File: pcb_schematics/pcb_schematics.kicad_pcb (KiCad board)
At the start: 2 copper layers, 100 x 100 mm, 73 parts, among them J1 Jack, J2 Conn_01x01_Pin, J3 Conn_01x05, J4 Conn_01x05, J5 Conn_01x05, SW1 SW_Push, U1 RPi_Pico_TH, U2 RDA5807M_Module, U3 LM386, U4 LM386

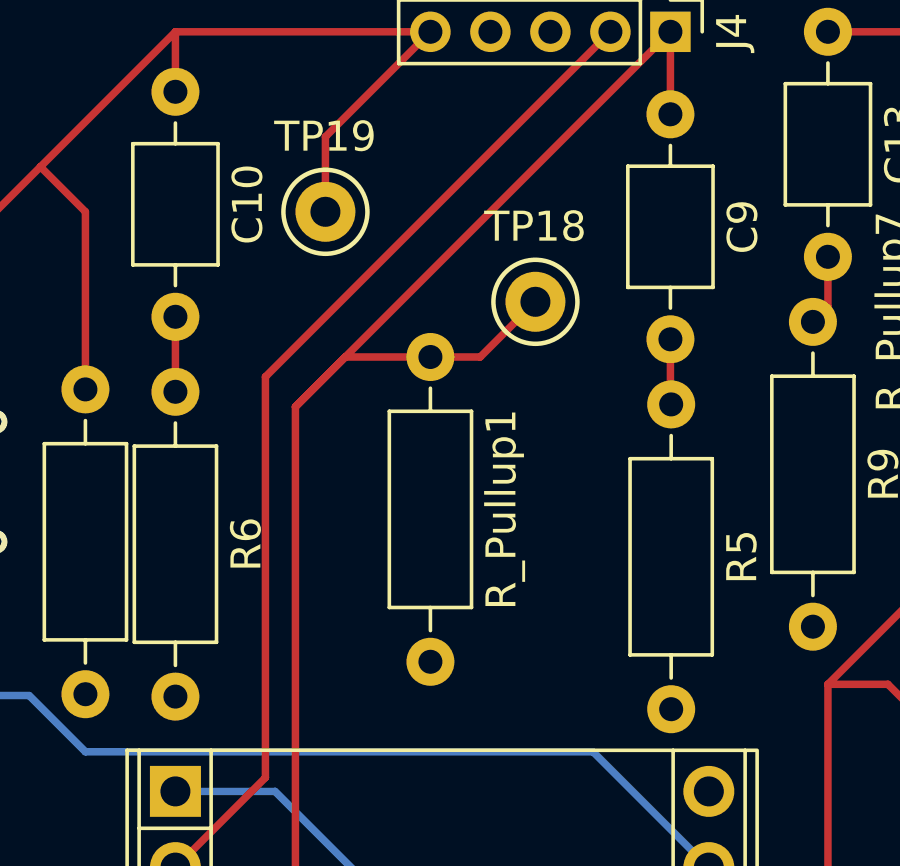
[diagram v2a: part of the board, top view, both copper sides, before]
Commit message: Accomodating usb cable
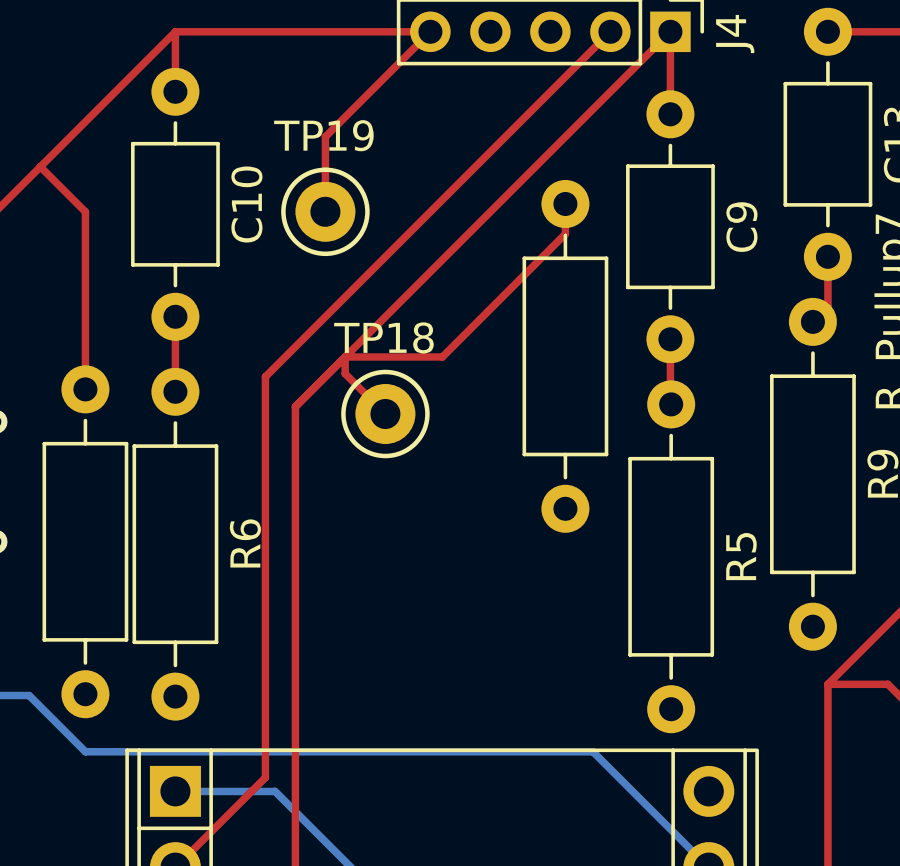
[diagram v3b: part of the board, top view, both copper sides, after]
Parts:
- J1: value Jack -> CUE_SJ1-352XNG
- moved R_Pullup1 6.80 mm to (153.0, 51.0)
- moved TP18 6.24 mm to (147.0, 58.0)
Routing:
- net /ROT1B: track 51.8 -> 57.2 mm
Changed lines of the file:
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@@
   )
   (footprint "TestPoint:TestPoint_Keystone_5000-5004_Miniature" (layer "F.Cu")
-    (at 152 54.26)
+    (at 147 58)
     (descr "Keystone Miniature THM Test Point 5000-5004, http://www.keyelco.com/product-pdf.cfm?p=1309")
     (tags "Through Hole Mount Test Points")
@@
   )
   (footprint "Resistor_THT:R_Axial_DIN0207_L6.3mm_D2.5mm_P10.16mm_Horizontal" (layer "F.Cu")
-    (at 148.5 56.1 -90)
+    (at 153 51 -90)
     (descr "Resistor, Axial_DIN0207 series, Axial, Horizontal, pin pitch=10.16mm, 0.25W = 1/4W, length*diameter=6.3*2.5mm^2, http://cdn-reichelt.de/documents/datenblatt/B400/1_4W%23YAG.pdf")
     (tags "Resistor Axial_DIN0207 series Axial Horizontal pin pitch 10.16mm 0.25W = 1/4W length 6.3mm diameter 2.5mm")
@@
     (property "ki_keywords" "R res resistor")
     (attr through_hole)
-    (fp_text reference "R_Pullup1" (at 5.08 -2.37 90) (layer "F.SilkS")
+    (fp_text reference "R_Pullup1" (at 5.08 -2.37 90) (layer "F.SilkS") hide
         (effects (font (size 1 1) (thickness 0.15)))
     )
@@
         (effects (font (size 1.016 1.016) (thickness 0.1524)) (justify mirror))
     )
-    (fp_text value "Jack" (at 0.5 -8) (layer "B.Fab")
+    (fp_text value "CUE_SJ1-352XNG" (at 0.5 -8) (layer "B.Fab")
         (effects (font (size 1.016 1.016) (thickness 0.1524)) (justify mirror))
     )
@@
   (segment (start 106.25 67.26) (end 106.25 61.51) (width 0.25) (layer "B.Cu") (net 51))
   (segment (start 109.5 58.26) (end 109.5 53.26) (width 0.25) (layer "B.Cu") (net 51))
+  (segment (start 145.66 56.1) (end 144 57.76) (width 0.25) (layer "F.Cu") (net 52))
   (segment (start 156.5 48.01) (end 156.5 45.26) (width 0.25) (layer "F.Cu") (net 52))
   (segment (start 156.5 45.26) (end 144 57.76) (width 0.25) (layer "F.Cu") (net 52))
-  (segment (start 144 57.76) (end 145.66 56.1) (width 0.25) (layer "F.Cu") (net 52))
-  (segment (start 150.16 56.1) (end 148.5 56.1) (width 0.25) (layer "F.Cu") (net 52))
-  (segment (start 152 54.26) (end 150.16 56.1) (width 0.25) (layer "F.Cu") (net 52))
   (segment (start 144 57.76) (end 144 74.136396) (width 0.25) (layer "F.Cu") (net 52))
+  (segment (start 147 58) (end 145.66 56.66) (width 0.25) (layer "F.Cu") (net 52))
+  (segment (start 153 51) (end 153 52) (width 0.25) (layer "F.Cu") (net 52))
+  (segment (start 153 52) (end 148.9 56.1) (width 0.25) (layer "F.Cu") (net 52))
+  (segment (start 145.66 56.66) (end 145.66 56.1) (width 0.25) (layer "F.Cu") (net 52))
+  (segment (start 148.9 56.1) (end 145.66 56.1) (width 0.25) (layer "F.Cu") (net 52))
   (segment (start 140.296396 77.84) (end 140 77.84) (width 0.25) (layer "F.Cu") (net 52))
   (segment (start 144 74.136396) (end 140.296396 77.84) (width 0.25) (layer "F.Cu") (net 52))
-  (segment (start 145.66 56.1) (end 148.5 56.1) (width 0.25) (layer "F.Cu") (net 52))
   (segment (start 156.5 55.51) (end 156.5 57.654763) (width 0.25) (layer "F.Cu") (net 53))
   (segment (start 156.5 57.654763) (end 156.525236 57.679999) (width 0.25) (layer "F.Cu") (net 53))

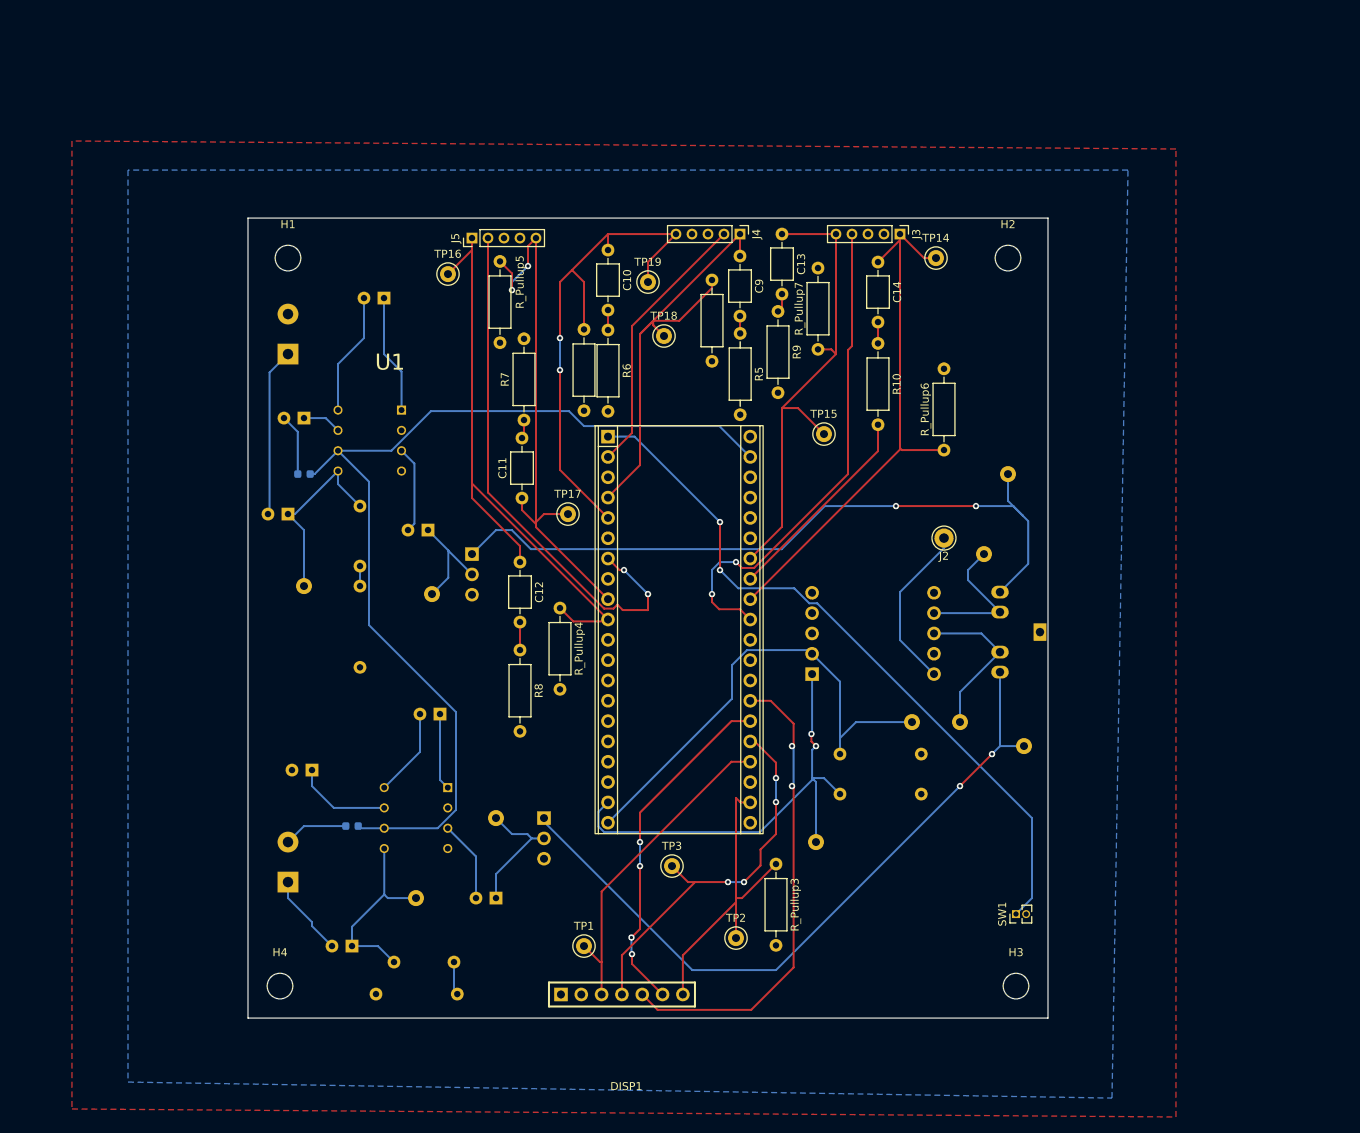
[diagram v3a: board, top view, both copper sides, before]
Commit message: completes third version of PCB
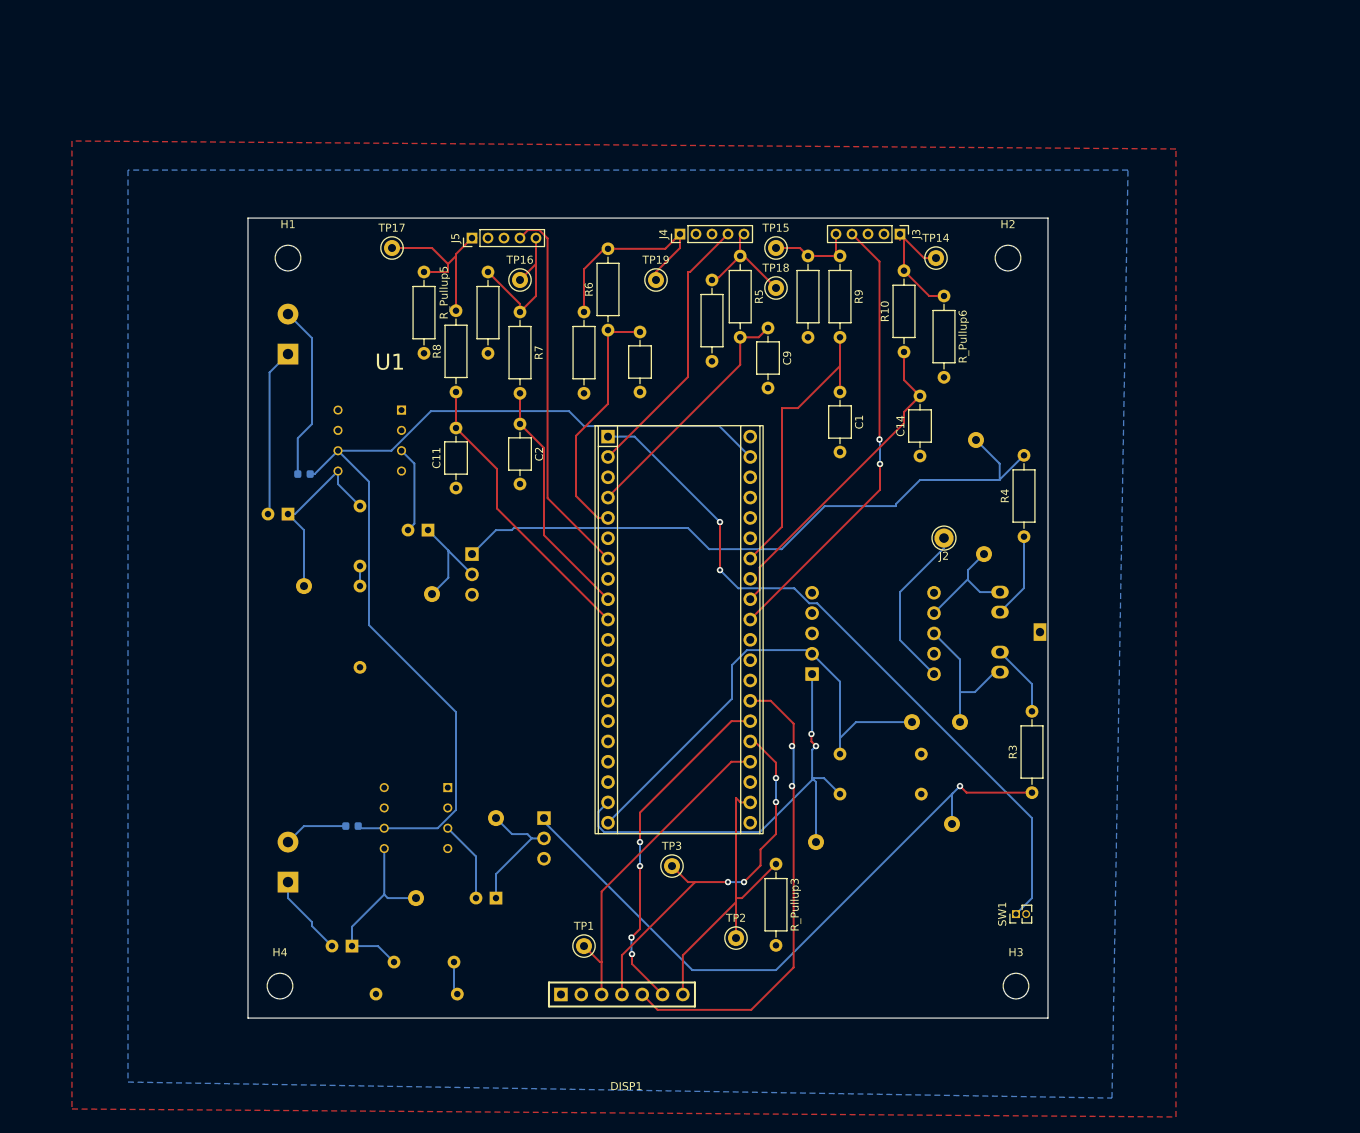
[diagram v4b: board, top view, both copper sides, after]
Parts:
- removed C12, C13: 0.05 µF, Capacitor_THT:C_Axial_L3.8mm_D2.6mm_P7.50mm_Horizontal
- removed C17, C18: 10 µF, Capacitor_THT:CP_Radial_D6.3mm_P2.50mm
- added R3: 10 k, Resistor_THT:R_Axial_DIN0207_L6.3mm_D2.5mm_P10.16mm_Horizontal, F.Cu at (193.0, 115.1)
- added R4: 10 k, Resistor_THT:R_Axial_DIN0207_L6.3mm_D2.5mm_P10.16mm_Horizontal, F.Cu at (192.0, 83.1)
- C1, C2: value 10 µF -> 0.05 µF; footprint Capacitor_THT:CP_Radial_D6.3mm_P2.50mm -> Capacitor_THT:C_Axial_L3.8mm_D2.6mm_P7.50mm_Horizontal; moved to F.Cu
- moved C1 81.2 mm to (169.0, 65.0), turned to -90 degrees
- moved R_Pullup4 43.0 mm to (125.0, 50.0)
- moved TP17 39.9 mm to (113.0, 47.0)
- moved R8 33.2 mm to (121.0, 65.0), turned to 90 degrees
- moved C2 27.0 mm to (129.0, 69.0), turned to -90 degrees
- moved C14 24.8 mm to (179.0, 73.0), turned to 90 degrees
- moved TP15 24.0 mm to (161.0, 47.0)
- moved R_Pullup6 19.3 mm to (182.0, 53.0), turned to -90 degrees
- moved C10 18.2 mm to (144.0, 65.0), turned to 90 degrees
- moved TP18 15.2 mm to (161.0, 52.0)
- moved R7 13.5 mm to (129.0, 55.0), turned to -90 degrees
- moved TP13 13.3 mm to (183.0, 119.0)
- moved R_Pullup7 11.7 mm to (165.0, 48.0), turned to -90 degrees
- moved R9 10.4 mm to (169.0, 48.0)
- moved R5 9.68 mm to (156.5, 48.0)
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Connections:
- C1 pad 1: Net-(U3-BYPASS) -> /ROT3A
- C10 pad 1: /ROT1A -> GND
- C10 pad 2: Net-(C10-Pad2) -> /ROT1A
- C11 pad 1: /ROT2A -> GND
- C11 pad 2: Net-(C11-Pad2) -> /ROT2B
- C14 pad 1: /ROT3B -> GND
- C14 pad 2: Net-(C14-Pad2) -> /ROT3B
- C2 pad 1: Net-(U4-BYPASS) -> /ROT2A
- C9 pad 2: Net-(C9-Pad2) -> GND
- J1 pad 2: /RSpeaker -> /LOUT
- J1 pad 3: /LSpeaker -> /ROUT
- J1 pad 4: /ROUT -> /RSpeaker
- J1 pad 5: /LOUT -> /LSpeaker
- J3 pad 1: /ROT3B -> Net-(J3-Pin_1)
- J3 pad 5: /ROT3A -> Net-(J3-Pin_5)
- J4 pad 1: /ROT1B -> Net-(J4-Pin_1)
- J4 pad 2: /SW2 -> GND
- J4 pad 4: GND -> /SW2
- J4 pad 5: /ROT1A -> Net-(J4-Pin_5)
- J5 pad 1: /ROT2B -> Net-(J5-Pin_1)
- J5 pad 2: /SW4 -> GND
- J5 pad 4: GND -> /SW4
- J5 pad 5: /ROT2A -> Net-(J5-Pin_5)
- R10 pad 1: Net-(C14-Pad2) -> /ROT3B
- R10 pad 2: GND -> Net-(J3-Pin_1)
- R5 pad 1: Net-(C9-Pad2) -> Net-(J4-Pin_5)
- R5 pad 2: GND -> /ROT1B
- R6 pad 1: Net-(C10-Pad2) -> /ROT1A
- R6 pad 2: GND -> Net-(J4-Pin_1)
- R7 pad 1: Net-(C11-Pad2) -> Net-(J5-Pin_5)
- R7 pad 2: GND -> /ROT2A
- R8 pad 1: Net-(C12-Pad2) -> /ROT2B
- R8 pad 2: GND -> Net-(J5-Pin_1)
- R9 pad 1: Net-(C13-Pad2) -> Net-(J3-Pin_5)
- R9 pad 2: GND -> /ROT3A
- RV1 pad 1: /LSpeaker -> Net-(R3-Pad1)
- RV2 pad 1: /RSpeaker -> Net-(R4-Pad2)
- R_Pullup1 pad 1: /ROT1B -> Net-(J4-Pin_5)
- R_Pullup2 pad 1: /ROT1A -> Net-(J4-Pin_1)
- R_Pullup4 pad 1: /ROT2B -> Net-(J5-Pin_5)
- R_Pullup5 pad 1: /ROT2A -> Net-(J5-Pin_1)
- R_Pullup6 pad 1: /ROT3B -> Net-(J3-Pin_1)
- R_Pullup7 pad 1: /ROT3A -> Net-(J3-Pin_5)
- TP12 pad 1: /RSpeaker -> Net-(R4-Pad2)
- TP13 pad 1: /LSpeaker -> Net-(R3-Pad1)
- TP14 pad 1: /ROT3B -> Net-(J3-Pin_1)
- TP15 pad 1: /ROT3A -> Net-(J3-Pin_5)
- TP16 pad 1: /ROT2B -> Net-(J5-Pin_5)
- TP17 pad 1: /ROT2A -> Net-(J5-Pin_1)
- TP18 pad 1: /ROT1B -> Net-(J4-Pin_5)
- TP19 pad 1: /ROT1A -> Net-(J4-Pin_1)
- U3 pad 1: Net-(C17-Pad1) -> unconnected-(U3-GAIN-Pad1)
- U3 pad 7: Net-(U3-BYPASS) -> unconnected-(U3-BYPASS-Pad7)
- U3 pad 8: Net-(C17-Pad2) -> unconnected-(U3-GAIN-Pad8)
- U4 pad 1: Net-(C18-Pad1) -> unconnected-(U4-GAIN-Pad1)
- U4 pad 7: Net-(U4-BYPASS) -> unconnected-(U4-BYPASS-Pad7)
- U4 pad 8: Net-(C18-Pad2) -> unconnected-(U4-GAIN-Pad8)
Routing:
- net Net-(R3-Pad1): track 0.00 -> 82.9 mm, vias 0 -> 1
- net Net-(R4-Pad2): track 0.00 -> 82.6 mm
- net /RSpeaker: track 91.0 -> 10.9 mm, vias 2 -> 0
- net /LSpeaker: track 89.0 -> 9.07 mm, vias 2 -> 0
- net /ROT2B: track 79.6 -> 36.6 mm
- net /ROT2A: track 69.2 -> 30.3 mm, vias 2 -> 0
- net /ROT1A: track 66.4 -> 31.6 mm, vias 2 -> 0
- net /ROT3B: track 69.4 -> 40.5 mm
- net /ROT1B: track 57.2 -> 30.7 mm
- net Net-(J4-Pin_1): track 0.00 -> 25.7 mm
- net /ROT3A: track 60.8 -> 36.7 mm
- net Net-(J5-Pin_1): track 0.00 -> 23.9 mm
- net Net-(J5-Pin_5): track 0.00 -> 22.8 mm
- net /SW4: track 67.1 -> 47.4 mm, vias 2 -> 0
- net Net-(J3-Pin_1): track 0.00 -> 17.6 mm
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
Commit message: fixed issues mentioned by rob and brent
Fix iteration 1
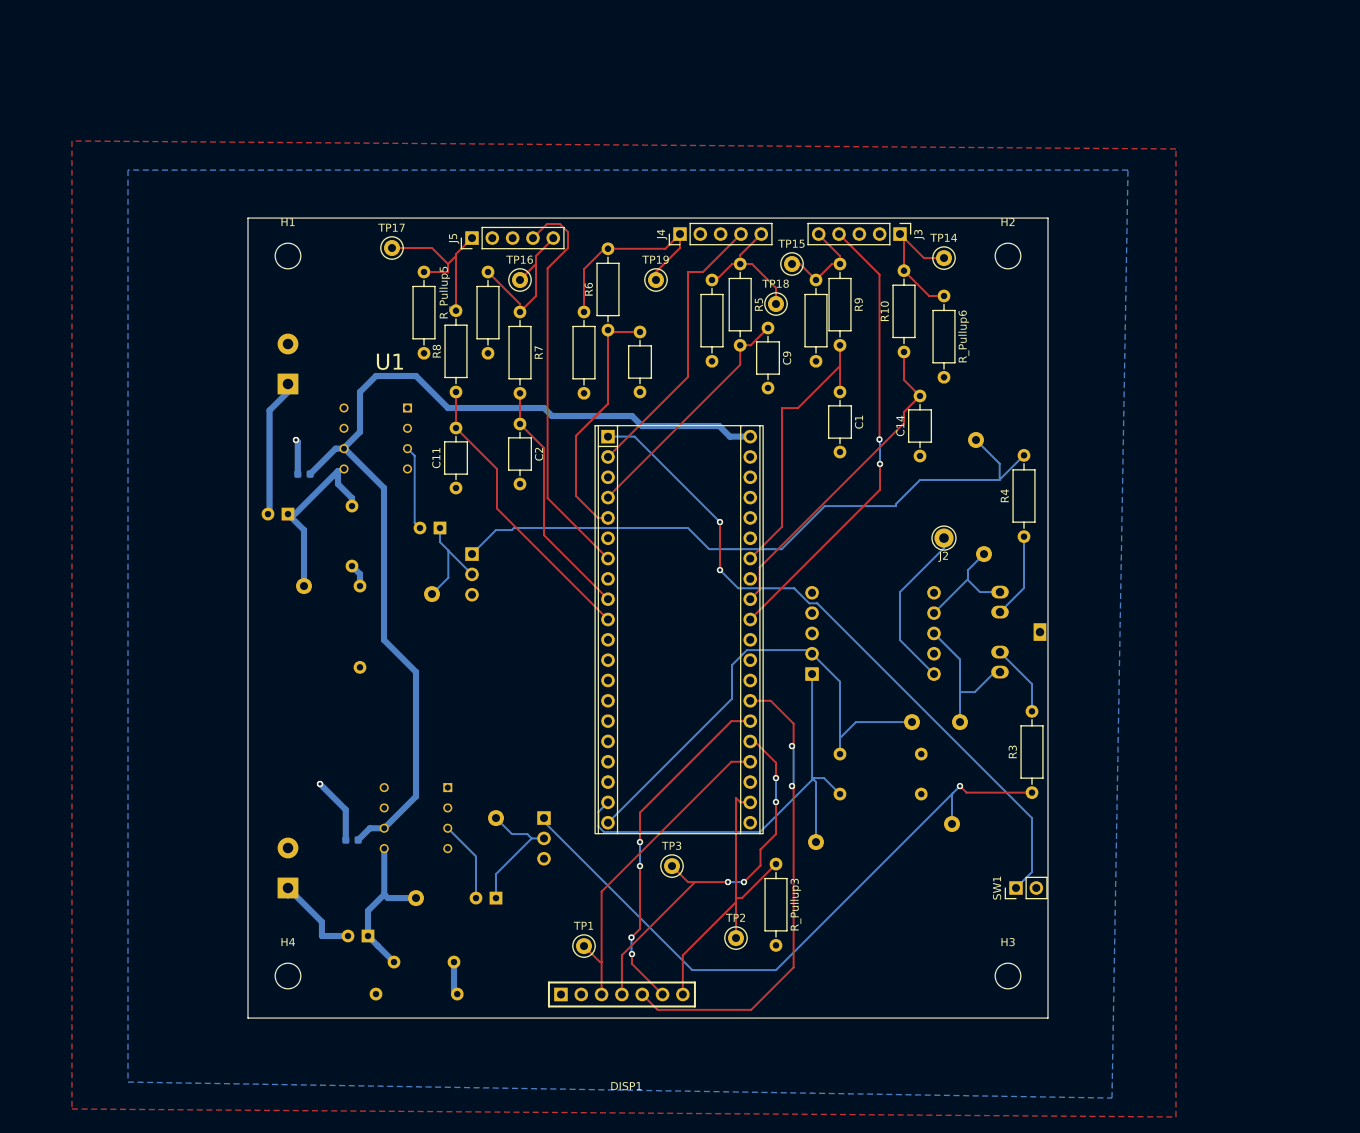
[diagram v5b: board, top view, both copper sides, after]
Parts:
- C1, C10, C11, C14, C2, C9: value 0.05 µF -> 0.01 µF
- J3, J4, J5: footprint Connector_PinHeader_2.00mm:PinHeader_1x05_P2.00mm_Vertical -> Connector_PinHeader_2.54mm:PinHeader_1x05_P2.54mm_Vertical
- R7, R8: value 10Ω -> 10kΩ
- R_Pullup1, R_Pullup2, R_Pullup3, R_Pullup4, R_Pullup5, R_Pullup6, R_Pullup7: value 2kΩ -> 10kΩ
- SW1: footprint Connector_PinHeader_1.27mm:PinHeader_1x02_P1.27mm_Vertical -> Connector_PinHeader_2.54mm:PinHeader_1x02_P2.54mm_Vertical
- moved LS2 3.74 mm to (100.0, 64.0)
- moved SW1 3.26 mm to (191.0, 127.0)
- moved R_Pullup7 3.16 mm to (166.0, 51.0)
- moved TP15 2.83 mm to (163.0, 49.0)
- moved C6 2.36 mm to (110.0, 133.0)
- moved TP18 2.00 mm to (161.0, 54.0)
- moved C8 1.74 mm to (108.0, 121.0)
- moved H3 1.61 mm to (190.0, 138.0)
- moved H4 1.61 mm to (100.0, 138.0)
- moved C16 1.52 mm to (119.0, 82.0)
- moved C4 1.00 mm to (108.0, 79.3)
- moved R5 1.00 mm to (156.5, 49.0)
- moved R9 1.00 mm to (169.0, 49.0)
- moved TP14 1.00 mm to (182.0, 48.3)
- moved U4 0.79 mm to (111.0, 70.8)
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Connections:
- C7 pad 2: 5V -> +5V
- C8 pad 2: 5V -> +5V
- U1 pad 39: 5V -> unconnected-(U1-VSYS-Pad39)
- U3 pad 6: 5V -> +5V
- U4 pad 6: 5V -> +5V
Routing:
- net 5V: track 124.9 -> 0.00 mm
- net +5V: track 0.00 -> 123.1 mm
- net GND: track 30.0 -> 13.7 mm, vias 0 -> 2
- net Net-(C3-Pad2): track 21.0 -> 17.3 mm
- net Net-(C5-Pad1): track 24.1 -> 20.5 mm
- net /SW1: track 89.1 -> 85.8 mm
- net Net-(J4-Pin_5): track 13.2 -> 16.5 mm
- net /SW4: track 47.4 -> 50.5 mm
- net Net-(J5-Pin_5): track 22.8 -> 20.4 mm
- net Net-(C6-Pad2): track 10.3 -> 12.3 mm
- net /SW2: track 34.2 -> 35.8 mm
- net Net-(J3-Pin_5): track 11.4 -> 12.5 mm
- net Net-(J3-Pin_1): track 17.6 -> 18.6 mm
- net /ROT3A: track 36.7 -> 35.7 mm
- net /SW3: track 56.5 -> 57.1 mm
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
